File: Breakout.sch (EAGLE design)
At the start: 7 parts

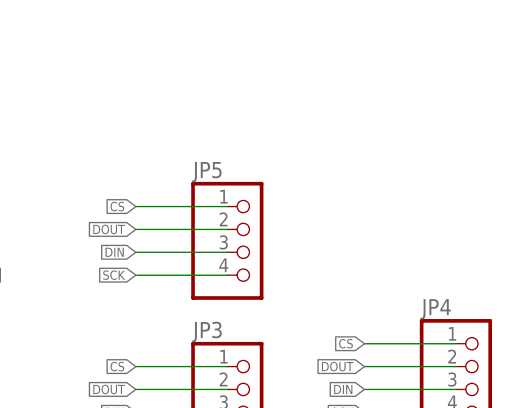
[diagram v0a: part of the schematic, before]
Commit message: Nudge layout to fit more squarely on mil grid
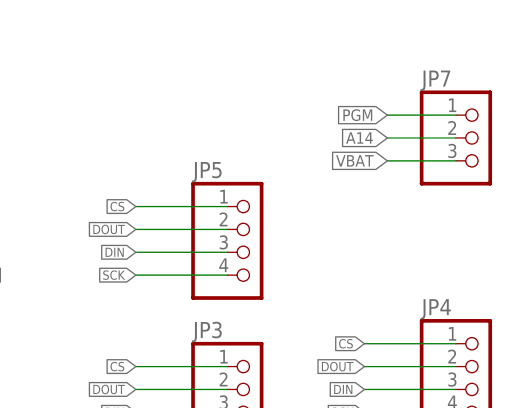
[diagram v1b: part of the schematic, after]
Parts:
- added JP7: (no value), pinhead:PINHD-1X3
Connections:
- net A14: now also JP7.2
- net PGM: now also JP7.1
- net VBAT: now also JP7.3
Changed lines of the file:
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@@
 <layer number="48" name="Document" color="7" fill="1" visible="no" active="no"/>
 <layer number="49" name="Reference" color="7" fill="1" visible="no" active="no"/>
+<layer number="50" name="dxf" color="7" fill="1" visible="no" active="no"/>
 <layer number="51" name="tDocu" color="14" fill="1" visible="no" active="no"/>
 <layer number="52" name="bDocu" color="7" fill="1" visible="no" active="no"/>
+<layer number="53" name="tGND_GNDA" color="7" fill="9" visible="no" active="no"/>
+<layer number="54" name="bGND_GNDA" color="1" fill="9" visible="no" active="no"/>
+<layer number="56" name="wert" color="7" fill="1" visible="no" active="no"/>
+<layer number="57" name="tCAD" color="7" fill="1" visible="no" active="no"/>
+<layer number="59" name="tCarbon" color="7" fill="1" visible="no" active="no"/>
+<layer number="60" name="bCarbon" color="7" fill="1" visible="no" active="no"/>
 <layer number="90" name="Modules" color="5" fill="1" visible="yes" active="yes"/>
 <layer number="91" name="Nets" color="2" fill="1" visible="yes" active="yes"/>
@@
 <layer number="97" name="Info" color="7" fill="1" visible="yes" active="yes"/>
 <layer number="98" name="Guide" color="6" fill="1" visible="yes" active="yes"/>
+<layer number="99" name="SpiceOrder" color="7" fill="1" visible="no" active="no"/>
+<layer number="100" name="Muster" color="7" fill="1" visible="no" active="no"/>
+<layer number="101" name="Patch_Top" color="12" fill="4" visible="yes" active="yes"/>
+<layer number="102" name="Vscore" color="7" fill="1" visible="yes" active="yes"/>
+<layer number="103" name="tMap" color="7" fill="1" visible="yes" active="yes"/>
+<layer number="104" name="Name" color="16" fill="1" visible="yes" active="yes"/>
+<layer number="105" name="tPlate" color="7" fill="1" visible="yes" active="yes"/>
+<layer number="106" name="bPlate" color="7" fill="1" visible="yes" active="yes"/>
+<layer number="107" name="Crop" color="7" fill="1" visible="yes" active="yes"/>
+<layer number="108" name="tplace-old" color="10" fill="1" visible="yes" active="yes"/>
+<layer number="109" name="ref-old" color="11" fill="1" visible="yes" active="yes"/>
+<layer number="110" name="fp0" color="7" fill="1" visible="yes" active="yes"/>
+<layer number="111" name="LPC17xx" color="7" fill="1" visible="yes" active="yes"/>
+<layer number="112" name="tSilk" color="7" fill="1" visible="yes" active="yes"/>
+<layer number="113" name="IDFDebug" color="4" fill="1" visible="yes" active="yes"/>
+<layer number="116" name="Patch_BOT" color="9" fill="4" visible="yes" active="yes"/>
+<layer number="121" name="_tsilk" color="7" fill="1" visible="yes" active="yes"/>
+<layer number="122" name="_bsilk" color="7" fill="1" visible="yes" active="yes"/>
+<layer number="123" name="tTestmark" color="7" fill="1" visible="yes" active="yes"/>
+<layer number="124" name="bTestmark" color="7" fill="1" visible="yes" active="yes"/>
+<layer number="125" name="_tNames" color="7" fill="1" visible="yes" active="yes"/>
+<layer number="126" name="_bNames" color="7" fill="1" visible="yes" active="yes"/>
+<layer number="127" name="_tValues" color="7" fill="1" visible="yes" active="yes"/>
+<layer number="128" name="_bValues" color="7" fill="1" visible="yes" active="yes"/>
+<layer number="129" name="Mask" color="7" fill="1" visible="yes" active="yes"/>
+<layer number="131" name="tAdjust" color="7" fill="1" visible="yes" active="yes"/>
+<layer number="132" name="bAdjust" color="7" fill="1" visible="yes" active="yes"/>
+<layer number="144" name="Drill_legend" color="7" fill="1" visible="yes" active="yes"/>
+<layer number="150" name="Notes" color="7" fill="1" visible="yes" active="yes"/>
+<layer number="151" name="HeatSink" color="7" fill="1" visible="yes" active="yes"/>
+<layer number="152" name="_bDocu" color="7" fill="1" visible="yes" active="yes"/>
+<layer number="153" name="FabDoc1" color="7" fill="1" visible="yes" active="yes"/>
+<layer number="154" name="FabDoc2" color="7" fill="1" visible="yes" active="yes"/>
+<layer number="155" name="FabDoc3" color="7" fill="1" visible="yes" active="yes"/>
+<layer number="199" name="Contour" color="7" fill="1" visible="yes" active="yes"/>
+<layer number="200" name="200bmp" color="1" fill="10" visible="yes" active="yes"/>
+<layer number="201" name="201bmp" color="2" fill="10" visible="yes" active="yes"/>
+<layer number="202" name="202bmp" color="3" fill="10" visible="yes" active="yes"/>
+<layer number="203" name="203bmp" color="4" fill="10" visible="yes" active="yes"/>
+<layer number="204" name="204bmp" color="5" fill="10" visible="yes" active="yes"/>
+<layer number="205" name="205bmp" color="6" fill="10" visible="yes" active="yes"/>
+<layer number="206" name="206bmp" color="7" fill="10" visible="yes" active="yes"/>
+<layer number="207" name="207bmp" color="8" fill="10" visible="yes" active="yes"/>
+<layer number="208" name="208bmp" color="9" fill="10" visible="yes" active="yes"/>
+<layer number="209" name="209bmp" color="7" fill="1" visible="yes" active="yes"/>
+<layer number="210" name="210bmp" color="7" fill="1" visible="yes" active="yes"/>
+<layer number="211" name="211bmp" color="7" fill="1" visible="yes" active="yes"/>
+<layer number="212" name="212bmp" color="7" fill="1" visible="yes" active="yes"/>
+<layer number="213" name="213bmp" color="7" fill="1" visible="yes" active="yes"/>
+<layer number="214" name="214bmp" color="7" fill="1" visible="yes" active="yes"/>
+<layer number="215" name="215bmp" color="7" fill="1" visible="yes" active="yes"/>
+<layer number="216" name="216bmp" color="7" fill="1" visible="yes" active="yes"/>
+<layer number="217" name="217bmp" color="18" fill="1" visible="no" active="no"/>
+<layer number="218" name="218bmp" color="19" fill="1" visible="no" active="no"/>
+<layer number="219" name="219bmp" color="20" fill="1" visible="no" active="no"/>
+<layer number="220" name="220bmp" color="21" fill="1" visible="no" active="no"/>
+<layer number="221" name="221bmp" color="22" fill="1" visible="no" active="no"/>
+<layer number="222" name="222bmp" color="23" fill="1" visible="no" active="no"/>
+<layer number="223" name="223bmp" color="24" fill="1" visible="no" active="no"/>
+<layer number="224" name="224bmp" color="25" fill="1" visible="no" active="no"/>
+<layer number="225" name="225bmp" color="7" fill="1" visible="yes" active="yes"/>
+<layer number="226" name="226bmp" color="7" fill="1" visible="yes" active="yes"/>
+<layer number="227" name="227bmp" color="7" fill="1" visible="yes" active="yes"/>
+<layer number="228" name="228bmp" color="7" fill="1" visible="yes" active="yes"/>
+<layer number="229" name="229bmp" color="7" fill="1" visible="yes" active="yes"/>
+<layer number="230" name="230bmp" color="7" fill="1" visible="yes" active="yes"/>
+<layer number="231" name="231bmp" color="7" fill="1" visible="yes" active="yes"/>
+<layer number="248" name="Housing" color="7" fill="1" visible="yes" active="yes"/>
+<layer number="249" name="Edge" color="7" fill="1" visible="yes" active="yes"/>
+<layer number="250" name="Descript" color="3" fill="1" visible="no" active="no"/>
+<layer number="251" name="SMDround" color="12" fill="11" visible="no" active="no"/>
+<layer number="254" name="cooling" color="7" fill="1" visible="yes" active="yes"/>
+<layer number="255" name="routoute" color="7" fill="1" visible="yes" active="yes"/>
 </layers>
 <schematic xreflabel="%F%N/%S.%C%R" xrefpart="/%S.%C%R">
@@
 <part name="JP4" library="pinhead" deviceset="PINHD-1X4" device=""/>
 <part name="JP6" library="pinhead" deviceset="PINHD-1X8" device=""/>
+<part name="JP7" library="pinhead" deviceset="PINHD-1X3" device=""/>
 </parts>
 <sheets>
@@
 <instance part="JP4" gate="A" x="157.48" y="45.72"/>
 <instance part="JP6" gate="A" x="132.08" y="12.7"/>
+<instance part="JP7" gate="A" x="157.48" y="73.66"/>
 </instances>
 <busses>
@@
 <label x="99.06" y="73.66" size="1.016" layer="95" xref="yes"/>
 </segment>
+<segment>
+<pinref part="JP7" gate="A" pin="3"/>
+<wire x1="154.94" y1="71.12" x2="147.32" y2="71.12" width="0.1524" layer="91"/>
+<label x="147.32" y="71.12" size="1.27" layer="95" rot="R180" xref="yes"/>
+</segment>
 </net>
 <net name="PGM" class="0">
@@
 <label x="99.06" y="66.04" size="1.016" layer="95" xref="yes"/>
 </segment>
+<segment>
+<pinref part="JP7" gate="A" pin="1"/>
+<wire x1="154.94" y1="76.2" x2="147.32" y2="76.2" width="0.1524" layer="91"/>
+<label x="147.32" y="76.2" size="1.27" layer="95" rot="R180" xref="yes"/>
+</segment>
 </net>
 <net name="A14" class="0">
@@
 <label x="99.06" y="53.34" size="1.016" layer="95" xref="yes"/>
 </segment>
-</net>
+<segment>
+<pinref part="JP7" gate="A" pin="2"/>
+<wire x1="147.32" y1="73.66" x2="154.94" y2="73.66" width="0.1524" layer="91"/>
+<label x="147.32" y="73.66" size="1.27" layer="95" rot="R180" xref="yes"/>
+</segment>
+</net>

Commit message: Add ALL the GNDs...
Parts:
- added JP8: (no value), pinhead:PINHD-1X3
- JP6: device pinhead:PINHD-1X8 -> pinhead:PINHD-1X10
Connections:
- net 3V: now also JP6.9
- net GND: now also JP6.10, JP8.1, JP8.2, JP8.3
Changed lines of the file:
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@@
 <part name="JP3" library="pinhead" deviceset="PINHD-1X4" device=""/>
 <part name="JP4" library="pinhead" deviceset="PINHD-1X4" device=""/>
-<part name="JP6" library="pinhead" deviceset="PINHD-1X8" device=""/>
+<part name="JP6" library="pinhead" deviceset="PINHD-1X10" device=""/>
 <part name="JP7" library="pinhead" deviceset="PINHD-1X3" device=""/>
+<part name="JP8" library="pinhead" deviceset="PINHD-1X3" device=""/>
+<part name="GND1" library="SparkFun-Aesthetics" deviceset="GND" device=""/>
 </parts>
 <sheets>
@@
 <instance part="JP6" gate="A" x="132.08" y="12.7"/>
 <instance part="JP7" gate="A" x="157.48" y="73.66"/>
+<instance part="JP8" gate="A" x="157.48" y="22.86"/>
+<instance part="GND1" gate="1" x="147.32" y="12.7"/>
 </instances>
 <busses>
@@
 <wire x1="129.54" y1="5.08" x2="121.92" y2="5.08" width="0.1524" layer="91"/>
 <label x="121.92" y="5.08" size="1.27" layer="95" rot="R180" xref="yes"/>
+<label x="121.92" y="0" size="1.27" layer="95" rot="R180" xref="yes"/>
+</segment>
+<segment>
+<pinref part="JP8" gate="A" pin="3"/>
+<pinref part="GND1" gate="1" pin="GND"/>
+<wire x1="154.94" y1="20.32" x2="147.32" y2="20.32" width="0.1524" layer="91"/>
+<wire x1="147.32" y1="20.32" x2="147.32" y2="15.24" width="0.1524" layer="91"/>
+<pinref part="JP8" gate="A" pin="2"/>
+<wire x1="154.94" y1="22.86" x2="147.32" y2="22.86" width="0.1524" layer="91"/>
+<wire x1="147.32" y1="22.86" x2="147.32" y2="20.32" width="0.1524" layer="91"/>
+<junction x="147.32" y="20.32"/>
+<pinref part="JP8" gate="A" pin="1"/>
+<wire x1="154.94" y1="25.4" x2="147.32" y2="25.4" width="0.1524" layer="91"/>
+<wire x1="147.32" y1="25.4" x2="147.32" y2="22.86" width="0.1524" layer="91"/>
+<junction x="147.32" y="22.86"/>
+</segment>
+<segment>
+<pinref part="JP6" gate="A" pin="10"/>
+<wire x1="129.54" y1="0" x2="121.92" y2="0" width="0.1524" layer="91"/>
 </segment>
 </net>
@@
 <wire x1="129.54" y1="7.62" x2="121.92" y2="7.62" width="0.1524" layer="91"/>
 <label x="121.92" y="7.62" size="1.27" layer="95" rot="R180" xref="yes"/>
-</segment>
-</net>
+<label x="121.92" y="2.54" size="1.27" layer="95" rot="R180" xref="yes"/>
+</segment>
+<segment>
+<pinref part="JP6" gate="A" pin="9"/>
+<wire x1="129.54" y1="2.54" x2="121.92" y2="2.54" width="0.1524" layer="91"/>
+</segment>
+</net>
